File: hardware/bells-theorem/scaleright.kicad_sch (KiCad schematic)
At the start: 19 parts, among them U19 TL074

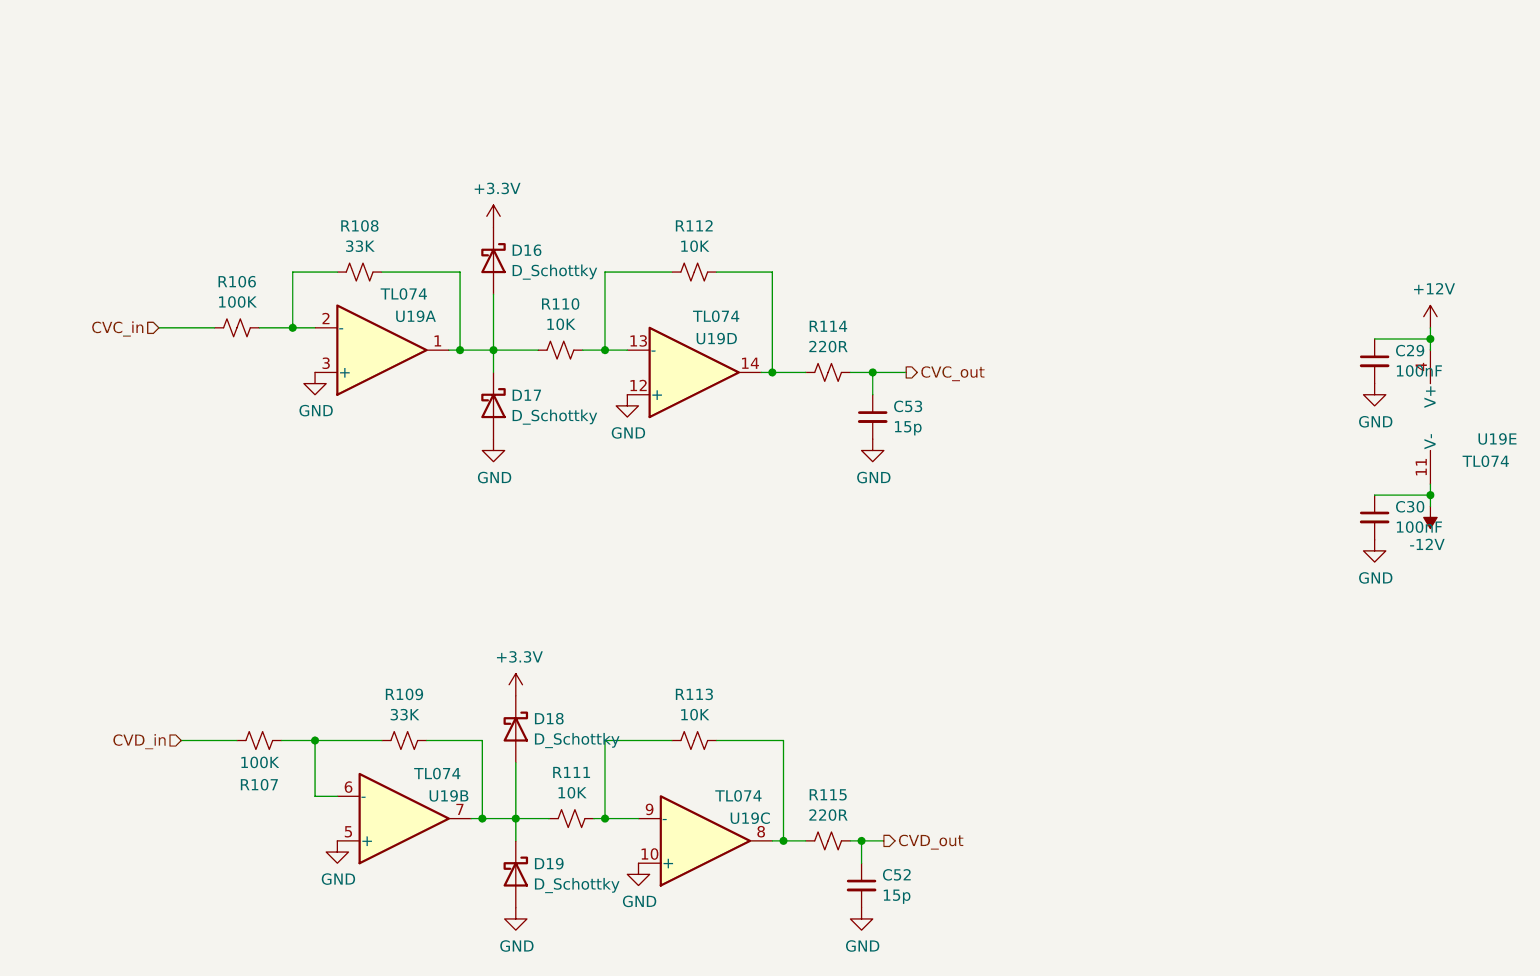
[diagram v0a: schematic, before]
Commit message: Modified with Jim M's recommendations for input scaling
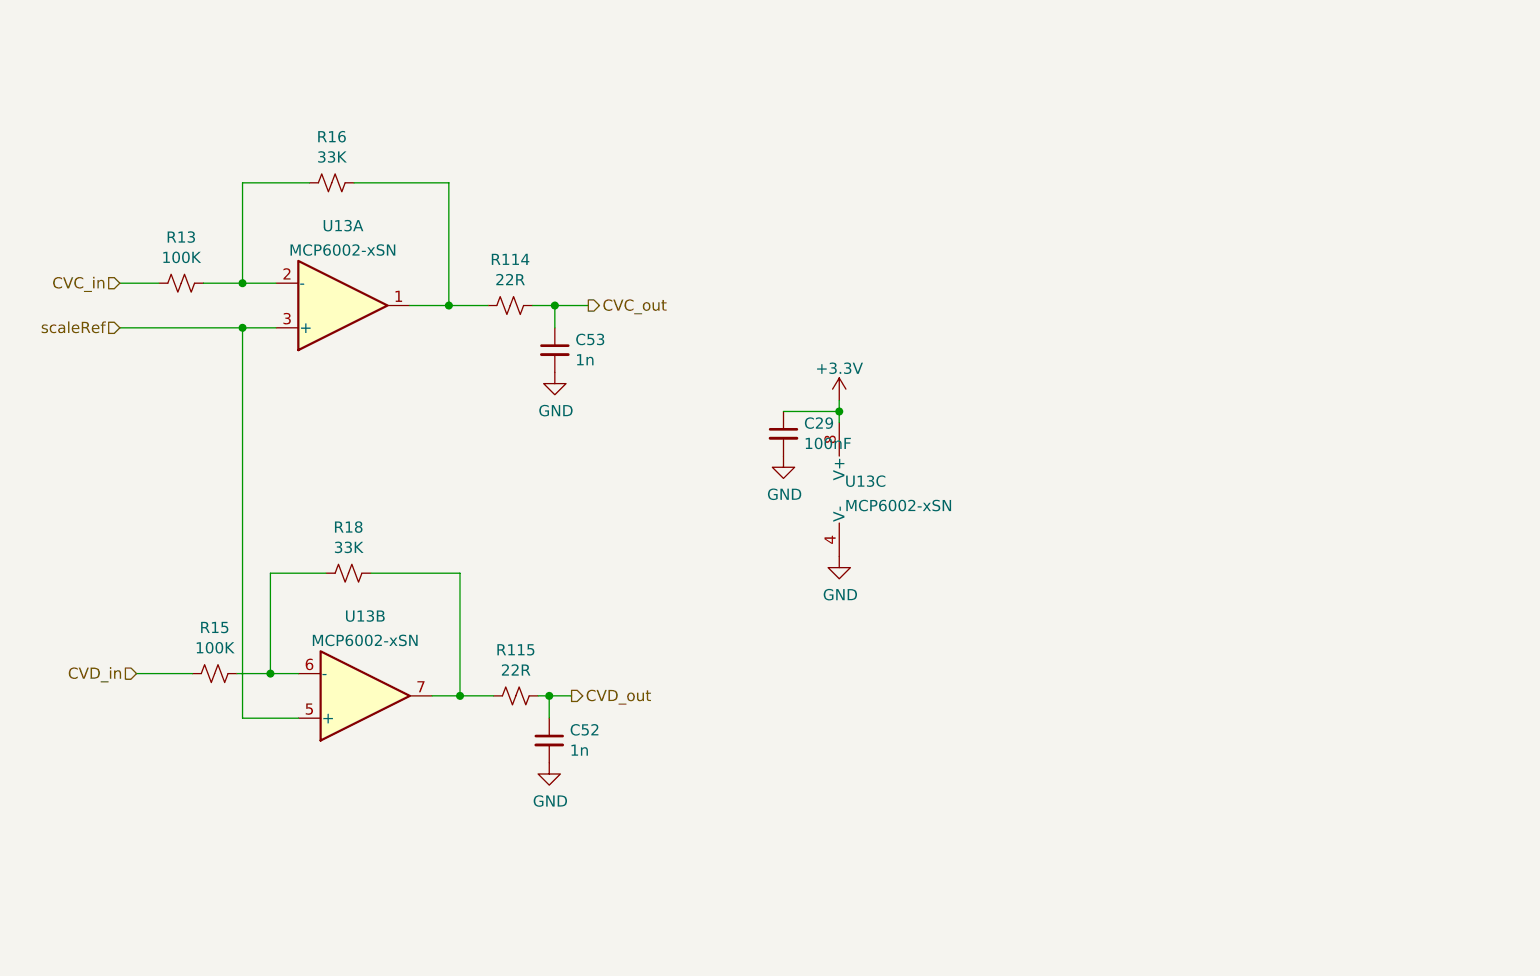
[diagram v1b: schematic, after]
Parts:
- removed C30: 100nF, Capacitor_SMD:C_0805_2012Metric_Pad1.15x1.40mm_HandSolder, symbol Device:C_Small
- removed D16, D17, D18, D19: D_Schottky, Resistor_SMD:R_0805_2012Metric_Pad1.15x1.40mm_HandSolder, symbol Device:D_Schottky
- removed R106, R107: 100K, Resistor_SMD:R_0805_2012Metric_Pad1.15x1.40mm_HandSolder, symbol Device:R_Small_US
- removed R108, R109: 33K, Resistor_SMD:R_0805_2012Metric_Pad1.15x1.40mm_HandSolder, symbol Device:R_Small_US
- removed R110, R111, R112, R113: 10K, Resistor_SMD:R_0805_2012Metric_Pad1.15x1.40mm_HandSolder, symbol Device:R_Small_US
- removed U19: TL074, Package_SO:SOIC-14_3.9x8.7mm_P1.27mm, symbol Amplifier_Operational:TL074
- added R13, R15: 100K, Resistor_SMD:R_0805_2012Metric_Pad1.15x1.40mm_HandSolder, symbol Device:R_Small_US
- added R16, R18: 33K, Resistor_SMD:R_0805_2012Metric_Pad1.15x1.40mm_HandSolder, symbol Device:R_Small_US
- added U13: MCP6002-xSN, symbol Amplifier_Operational:MCP6002-xSN
- C52, C53: value 15p -> 1n
- R114, R115: value 220R -> 22R
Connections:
- net +12V is gone; now on net +3V3: C29.1
- net +3V3: now also U13.8 (V+)
- net CVC_in: now also R13.2
- net CVD_in: now also R15.2
- net GND: now also U13.4 (V-)
- net at R114.2: now also R16.1, U13.1
- net at R115.2: now also R18.1, U13.7
- new net: R15.1, R18.2, U13.6 (-)
- new net: R13.1, R16.2, U13.2 (-)
- new net scaleRef: U13.3 (+), U13.5 (+)
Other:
- moved on the sheet: C29, C52, C53, R114, R115

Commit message: All changes up to date with latest revisions
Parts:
- C29: footprint Capacitor_SMD:C_0805_2012Metric_Pad1.15x1.40mm_HandSolder -> Capacitor_SMD:C_0805_2012Metric_Pad1.18x1.45mm_HandSolder
- R114, R115, R13, R15, R16, R18: footprint Resistor_SMD:R_0805_2012Metric_Pad1.15x1.40mm_HandSolder -> Resistor_SMD:R_0805_2012Metric_Pad1.20x1.40mm_HandSolder
- U13: footprint (none) -> Package_SO:SOIC-8_3.9x4.9mm_P1.27mm
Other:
- title: (none) -> Bell's Theorem
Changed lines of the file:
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@@
 (kicad_sch (version 20211123) (generator eeschema)
   (paper "A4")
+  (title_block
+    (title "Bell's Theorem")
+    (date "2022-01-16")
+  )
   (junction (at 111.76 50.8) (diameter 0) (color 0 0 0 0)
   )
@@
     (property "Reference" "R115" (id 0) (at 119.38 90.043 90))
     (property "Value" "22R" (id 1) (at 119.38 92.3544 90))
-    (property "Footprint" "Resistor_SMD:R_0805_2012Metric_Pad1.15x1.40mm_HandSolder" (id 2) (at 119.38 95.25 0)
+    (property "Footprint" "Resistor_SMD:R_0805_2012Metric_Pad1.20x1.40mm_HandSolder" (id 2) (at 119.38 95.25 0)
       (effects (font (size 1.27 1.27)) hide)
     )
@@
     (property "Reference" "R114" (id 0) (at 118.745 45.593 90))
     (property "Value" "22R" (id 1) (at 118.745 47.9044 90))
-    (property "Footprint" "Resistor_SMD:R_0805_2012Metric_Pad1.15x1.40mm_HandSolder" (id 2) (at 118.745 50.8 0)
+    (property "Footprint" "Resistor_SMD:R_0805_2012Metric_Pad1.20x1.40mm_HandSolder" (id 2) (at 118.745 50.8 0)
       (effects (font (size 1.27 1.27)) hide)
     )
@@
       (effects (font (size 1.27 1.27)) (justify left))
     )
-    (property "Footprint" "Capacitor_SMD:C_0805_2012Metric_Pad1.15x1.40mm_HandSolder" (id 2) (at 149.86 65.405 0)
+    (property "Footprint" "Capacitor_SMD:C_0805_2012Metric_Pad1.18x1.45mm_HandSolder" (id 2) (at 149.86 65.405 0)
       (effects (font (size 1.27 1.27)) hide)
     )
@@
     (property "Reference" "R18" (id 0) (at 100.33 76.073 90))
     (property "Value" "33K" (id 1) (at 100.33 78.3844 90))
-    (property "Footprint" "Resistor_SMD:R_0805_2012Metric_Pad1.15x1.40mm_HandSolder" (id 2) (at 100.33 81.28 0)
+    (property "Footprint" "Resistor_SMD:R_0805_2012Metric_Pad1.20x1.40mm_HandSolder" (id 2) (at 100.33 81.28 0)
       (effects (font (size 1.27 1.27)) hide)
     )
@@
       (effects (font (size 1.27 1.27)) (justify left))
     )
-    (property "Footprint" "" (id 2) (at 158.75 71.755 0)
+    (property "Footprint" "Package_SO:SOIC-8_3.9x4.9mm_P1.27mm" (id 2) (at 158.75 71.755 0)
       (effects (font (size 1.27 1.27)) hide)
     )
@@
     (property "Reference" "R16" (id 0) (at 98.425 31.623 90))
     (property "Value" "33K" (id 1) (at 98.425 33.9344 90))
-    (property "Footprint" "Resistor_SMD:R_0805_2012Metric_Pad1.15x1.40mm_HandSolder" (id 2) (at 98.425 36.83 0)
+    (property "Footprint" "Resistor_SMD:R_0805_2012Metric_Pad1.20x1.40mm_HandSolder" (id 2) (at 98.425 36.83 0)
       (effects (font (size 1.27 1.27)) hide)
     )
@@
     (property "Reference" "U13" (id 0) (at 99.695 41.7535 0))
     (property "Value" "MCP6002-xSN" (id 1) (at 99.695 44.5286 0))
-    (property "Footprint" "" (id 2) (at 99.695 50.8 0)
+    (property "Footprint" "Package_SO:SOIC-8_3.9x4.9mm_P1.27mm" (id 2) (at 99.695 50.8 0)
       (effects (font (size 1.27 1.27)) hide)
     )
@@
     (property "Reference" "R15" (id 0) (at 85.09 87.503 90))
     (property "Value" "100K" (id 1) (at 85.09 89.8144 90))
-    (property "Footprint" "Resistor_SMD:R_0805_2012Metric_Pad1.15x1.40mm_HandSolder" (id 2) (at 85.09 92.71 0)
+    (property "Footprint" "Resistor_SMD:R_0805_2012Metric_Pad1.20x1.40mm_HandSolder" (id 2) (at 85.09 92.71 0)
       (effects (font (size 1.27 1.27)) hide)
     )
@@
     (property "Reference" "U13" (id 0) (at 102.235 86.2035 0))
     (property "Value" "MCP6002-xSN" (id 1) (at 102.235 88.9786 0))
-    (property "Footprint" "" (id 2) (at 102.235 95.25 0)
+    (property "Footprint" "Package_SO:SOIC-8_3.9x4.9mm_P1.27mm" (id 2) (at 102.235 95.25 0)
       (effects (font (size 1.27 1.27)) hide)
     )
@@
     (property "Reference" "R13" (id 0) (at 81.28 43.053 90))
     (property "Value" "100K" (id 1) (at 81.28 45.3644 90))
-    (property "Footprint" "Resistor_SMD:R_0805_2012Metric_Pad1.15x1.40mm_HandSolder" (id 2) (at 81.28 48.26 0)
-      (effects (font (size 1.27 1.27)) hide)
-    )
+    (property "Footprint" "Resistor_SMD:R_0805_2012Metric_Pad1.20x1.40mm_HandSolder" (id 2) (at 81.28 48.26 0)
+      (effects (font (size 1.27 1.27)) hide)
+    )

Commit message: last hardware / software updates
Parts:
- R16, R18: value 33K -> 47K
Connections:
- net GND: now also R16.2, R18.2
- net at R115.2, U13.7: now also U13.6 (-); no longer R18.1
- net at R114.2, U13.1: now also U13.2 (-); no longer R16.1
- net scaleRef: no longer names the net of U13.5 (+)
- net scaleRef: now also R15.1, R18.1; no longer U13.3 (+)
- new net: R13.1, R16.1, U13.3 (+)
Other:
- moved on the sheet: R13, R15, R16, R18
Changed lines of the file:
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@@
   (junction (at 111.76 50.8) (diameter 0) (color 0 0 0 0)
   )
+  (junction (at 156.21 62.865) (diameter 0) (color 0 0 0 0)
+  )
+  (junction (at 123.19 95.25) (diameter 0) (color 0 0 0 0)
+  )
+  (junction (at 123.825 50.8) (diameter 0) (color 0 0 0 0)
+  )
+  (junction (at 90.805 97.79) (diameter 0) (color 0 0 0 0)
+  )
   (junction (at 88.265 53.34) (diameter 0) (color 0 0 0 0)
   )
-  (junction (at 156.21 62.865) (diameter 0) (color 0 0 0 0)
-  )
-  (junction (at 91.44 92.71) (diameter 0) (color 0 0 0 0)
-  )
-  (junction (at 123.19 95.25) (diameter 0) (color 0 0 0 0)
-  )
-  (junction (at 123.825 50.8) (diameter 0) (color 0 0 0 0)
-  )
   (junction (at 113.03 95.25) (diameter 0) (color 0 0 0 0)
   )
-  (junction (at 88.265 48.26) (diameter 0) (color 0 0 0 0)
-  )
   (wire (pts (xy 149.86 62.865) (xy 156.21 62.865))
     (stroke (width 0) (type default) (color 0 0 0 0))
   )
-  (wire (pts (xy 95.885 36.83) (xy 88.265 36.83))
-    (stroke (width 0) (type default) (color 0 0 0 0))
-  )
-  (wire (pts (xy 102.87 81.28) (xy 113.03 81.28))
+  (wire (pts (xy 91.44 81.28) (xy 113.03 81.28))
+    (stroke (width 0) (type default) (color 0 0 0 0))
+  )
+  (wire (pts (xy 90.805 97.79) (xy 90.805 100.33))
     (stroke (width 0) (type default) (color 0 0 0 0))
   )
@@
     (stroke (width 0) (type default) (color 0 0 0 0))
   )
-  (wire (pts (xy 88.265 53.34) (xy 88.265 97.79))
-    (stroke (width 0) (type default) (color 0 0 0 0))
-  )
-  (wire (pts (xy 83.82 48.26) (xy 88.265 48.26))
+  (wire (pts (xy 90.805 97.79) (xy 94.615 97.79))
     (stroke (width 0) (type default) (color 0 0 0 0))
   )
@@
     (stroke (width 0) (type default) (color 0 0 0 0))
   )
-  (wire (pts (xy 87.63 92.71) (xy 91.44 92.71))
-    (stroke (width 0) (type default) (color 0 0 0 0))
-  )
-  (wire (pts (xy 76.2 92.71) (xy 82.55 92.71))
+  (wire (pts (xy 76.835 97.79) (xy 83.185 97.79))
     (stroke (width 0) (type default) (color 0 0 0 0))
   )
@@
     (stroke (width 0) (type default) (color 0 0 0 0))
   )
-  (wire (pts (xy 74.295 48.26) (xy 78.74 48.26))
+  (wire (pts (xy 74.295 53.34) (xy 78.74 53.34))
     (stroke (width 0) (type default) (color 0 0 0 0))
   )
@@
     (stroke (width 0) (type default) (color 0 0 0 0))
   )
-  (wire (pts (xy 97.79 81.28) (xy 91.44 81.28))
-    (stroke (width 0) (type default) (color 0 0 0 0))
-  )
   (wire (pts (xy 113.03 81.28) (xy 113.03 95.25))
     (stroke (width 0) (type default) (color 0 0 0 0))
@@
     (stroke (width 0) (type default) (color 0 0 0 0))
   )
-  (wire (pts (xy 100.965 36.83) (xy 111.76 36.83))
-    (stroke (width 0) (type default) (color 0 0 0 0))
-  )
-  (wire (pts (xy 88.265 97.79) (xy 94.615 97.79))
+  (wire (pts (xy 88.265 36.83) (xy 111.76 36.83))
+    (stroke (width 0) (type default) (color 0 0 0 0))
+  )
+  (wire (pts (xy 88.265 97.79) (xy 90.805 97.79))
     (stroke (width 0) (type default) (color 0 0 0 0))
   )
@@
     (stroke (width 0) (type default) (color 0 0 0 0))
   )
+  (wire (pts (xy 83.82 53.34) (xy 88.265 53.34))
+    (stroke (width 0) (type default) (color 0 0 0 0))
+  )
+  (wire (pts (xy 123.19 95.25) (xy 121.92 95.25))
+    (stroke (width 0) (type default) (color 0 0 0 0))
+  )
+  (wire (pts (xy 113.03 95.25) (xy 116.84 95.25))
+    (stroke (width 0) (type default) (color 0 0 0 0))
+  )
+  (wire (pts (xy 88.265 48.26) (xy 92.075 48.26))
+    (stroke (width 0) (type default) (color 0 0 0 0))
+  )
+  (wire (pts (xy 111.76 50.8) (xy 116.205 50.8))
+    (stroke (width 0) (type default) (color 0 0 0 0))
+  )
   (wire (pts (xy 88.265 53.34) (xy 92.075 53.34))
     (stroke (width 0) (type default) (color 0 0 0 0))
   )
-  (wire (pts (xy 74.295 53.34) (xy 88.265 53.34))
-    (stroke (width 0) (type default) (color 0 0 0 0))
-  )
-  (wire (pts (xy 123.19 95.25) (xy 121.92 95.25))
-    (stroke (width 0) (type default) (color 0 0 0 0))
-  )
-  (wire (pts (xy 113.03 95.25) (xy 116.84 95.25))
-    (stroke (width 0) (type default) (color 0 0 0 0))
-  )
-  (wire (pts (xy 88.265 48.26) (xy 92.075 48.26))
-    (stroke (width 0) (type default) (color 0 0 0 0))
-  )
-  (wire (pts (xy 111.76 50.8) (xy 116.205 50.8))
+  (wire (pts (xy 88.265 53.34) (xy 88.265 56.515))
     (stroke (width 0) (type default) (color 0 0 0 0))
   )
@@
     (effects (font (size 1.27 1.27)) (justify left))
   )
-  (hierarchical_label "scaleRef" (shape input) (at 74.295 53.34 180)
-    (effects (font (size 1.27 1.27)) (justify right))
-  )
-  (hierarchical_label "CVD_in" (shape input) (at 76.2 92.71 180)
+  (hierarchical_label "CVD_in" (shape input) (at 76.835 97.79 180)
     (effects (font (size 1.27 1.27)) (justify right))
   )
@@
     (effects (font (size 1.27 1.27)) (justify left))
   )
-  (hierarchical_label "CVC_in" (shape input) (at 74.295 48.26 180)
+  (hierarchical_label "CVC_in" (shape input) (at 74.295 53.34 180)
     (effects (font (size 1.27 1.27)) (justify right))
   )
@@
     (pin "1")
   )
-  (symbol (lib_id "Device:R_Small_US") (at 100.33 81.28 270) (unit 1)
-    (in_bom yes) (on_board yes)
-    (property "Reference" "R18" (id 0) (at 100.33 76.073 90))
-    (property "Value" "33K" (id 1) (at 100.33 78.3844 90))
-    (property "Footprint" "Resistor_SMD:R_0805_2012Metric_Pad1.20x1.40mm_HandSolder" (id 2) (at 100.33 81.28 0)
-      (effects (font (size 1.27 1.27)) hide)
-    )
-    (property "Datasheet" "~" (id 3) (at 100.33 81.28 0)
+  (symbol (lib_id "power:GND") (at 90.805 105.41 0) (unit 1)
+    (in_bom yes) (on_board yes)
+    (property "Reference" "#PWR0167" (id 0) (at 90.805 111.76 0)
+      (effects (font (size 1.27 1.27)) hide)
+    )
+    (property "Value" "GND" (id 1) (at 90.932 109.8042 0))
+    (property "Footprint" "" (id 2) (at 90.805 105.41 0)
+      (effects (font (size 1.27 1.27)) hide)
+    )
+    (property "Datasheet" "" (id 3) (at 90.805 105.41 0)
+      (effects (font (size 1.27 1.27)) hide)
+    )
+    (pin "1")
+  )
+  (symbol (lib_id "Device:R_Small_US") (at 90.805 102.87 0) (unit 1)
+    (in_bom yes) (on_board yes)
+    (property "Reference" "R18" (id 0) (at 85.598 102.87 90))
+    (property "Value" "47K" (id 1) (at 87.9094 102.87 90))
+    (property "Footprint" "Resistor_SMD:R_0805_2012Metric_Pad1.20x1.40mm_HandSolder" (id 2) (at 90.805 102.87 0)
+      (effects (font (size 1.27 1.27)) hide)
+    )
+    (property "Datasheet" "~" (id 3) (at 90.805 102.87 0)
       (effects (font (size 1.27 1.27)) hide)
     )
@@
     (pin "8")
   )
-  (symbol (lib_id "Device:R_Small_US") (at 98.425 36.83 270) (unit 1)
-    (in_bom yes) (on_board yes)
-    (property "Reference" "R16" (id 0) (at 98.425 31.623 90))
-    (property "Value" "33K" (id 1) (at 98.425 33.9344 90))
-    (property "Footprint" "Resistor_SMD:R_0805_2012Metric_Pad1.20x1.40mm_HandSolder" (id 2) (at 98.425 36.83 0)
-      (effects (font (size 1.27 1.27)) hide)
-    )
-    (property "Datasheet" "~" (id 3) (at 98.425 36.83 0)
+  (symbol (lib_id "Device:R_Small_US") (at 88.265 59.055 0) (unit 1)
+    (in_bom yes) (on_board yes)
+    (property "Reference" "R16" (id 0) (at 83.058 59.055 90))
+    (property "Value" "47K" (id 1) (at 85.3694 59.055 90))
+    (property "Footprint" "Resistor_SMD:R_0805_2012Metric_Pad1.20x1.40mm_HandSolder" (id 2) (at 88.265 59.055 0)
+      (effects (font (size 1.27 1.27)) hide)
+    )
+    (property "Datasheet" "~" (id 3) (at 88.265 59.055 0)
       (effects (font (size 1.27 1.27)) hide)
     )
@@
     (pin "3")
   )
-  (symbol (lib_id "Device:R_Small_US") (at 85.09 92.71 270) (unit 1)
-    (in_bom yes) (on_board yes)
-    (property "Reference" "R15" (id 0) (at 85.09 87.503 90))
-    (property "Value" "100K" (id 1) (at 85.09 89.8144 90))
-    (property "Footprint" "Resistor_SMD:R_0805_2012Metric_Pad1.20x1.40mm_HandSolder" (id 2) (at 85.09 92.71 0)
-      (effects (font (size 1.27 1.27)) hide)
-    )
-    (property "Datasheet" "~" (id 3) (at 85.09 92.71 0)
+  (symbol (lib_id "Device:R_Small_US") (at 85.725 97.79 270) (unit 1)
+    (in_bom yes) (on_board yes)
+    (property "Reference" "R15" (id 0) (at 85.725 92.583 90))
+    (property "Value" "100K" (id 1) (at 85.725 94.8944 90))
+    (property "Footprint" "Resistor_SMD:R_0805_2012Metric_Pad1.20x1.40mm_HandSolder" (id 2) (at 85.725 97.79 0)
+      (effects (font (size 1.27 1.27)) hide)
+    )
+    (property "Datasheet" "~" (id 3) (at 85.725 97.79 0)
       (effects (font (size 1.27 1.27)) hide)
     )
@@
     (pin "1")
   )
-  (symbol (lib_id "Device:R_Small_US") (at 81.28 48.26 270) (unit 1)
-    (in_bom yes) (on_board yes)
-    (property "Reference" "R13" (id 0) (at 81.28 43.053 90))
-    (property "Value" "100K" (id 1) (at 81.28 45.3644 90))
-    (property "Footprint" "Resistor_SMD:R_0805_2012Metric_Pad1.20x1.40mm_HandSolder" (id 2) (at 81.28 48.26 0)
-      (effects (font (size 1.27 1.27)) hide)
-    )
-    (property "Datasheet" "~" (id 3) (at 81.28 48.26 0)
-      (effects (font (size 1.27 1.27)) hide)
-    )
-    (pin "1")
-    (pin "2")
+  (symbol (lib_id "Device:R_Small_US") (at 81.28 53.34 270) (unit 1)
+    (in_bom yes) (on_board yes)
+    (property "Reference" "R13" (id 0) (at 81.28 48.133 90))
+    (property "Value" "100K" (id 1) (at 81.28 50.4444 90))
+    (property "Footprint" "Resistor_SMD:R_0805_2012Metric_Pad1.20x1.40mm_HandSolder" (id 2) (at 81.28 53.34 0)
+      (effects (font (size 1.27 1.27)) hide)
+    )
+    (property "Datasheet" "~" (id 3) (at 81.28 53.34 0)
+      (effects (font (size 1.27 1.27)) hide)
+    )
+    (pin "1")
+    (pin "2")
+  )
+  (symbol (lib_id "power:GND") (at 88.265 61.595 0) (unit 1)
+    (in_bom yes) (on_board yes)
+    (property "Reference" "#PWR0166" (id 0) (at 88.265 67.945 0)
+      (effects (font (size 1.27 1.27)) hide)
+    )
+    (property "Value" "GND" (id 1) (at 88.392 65.9892 0))
+    (property "Footprint" "" (id 2) (at 88.265 61.595 0)
+      (effects (font (size 1.27 1.27)) hide)
+    )
+    (property "Datasheet" "" (id 3) (at 88.265 61.595 0)
+      (effects (font (size 1.27 1.27)) hide)
+    )
+    (pin "1")
   )
 )
